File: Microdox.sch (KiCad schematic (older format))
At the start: 47 parts, among them P1 USB, P2 CONN_01X03, SW0:0 SWITCH_DIODE, SW0:1 SWITCH_DIODE, SW0:2 SWITCH_DIODE, SW0:3 SWITCH_DIODE, SW0:4 SWITCH_DIODE, SW0:5 SWITCH_DIODE, SW0:6 SWITCH_DIODE, SW1:0 SWITCH_DIODE, SW1:1 SWITCH_DIODE, SW1:2 SWITCH_DIODE, SW1:3 SWITCH_DIODE, SW1:4 SWITCH_DIODE, SW1:5 SWITCH_DIODE, SW2:0 SWITCH_DIODE, SW2:1 SWITCH_DIODE, SW2:2 SWITCH_DIODE, SW2:3 SWITCH_DIODE, SW2:4 SWITCH_DIODE, SW2:5 SWITCH_DIODE, SW2:6 SWITCH_DIODE, SW3:0 SWITCH_DIODE, SW3:1 SWITCH_DIODE, SW3:2 SWITCH_DIODE, SW3:3 SWITCH_DIODE, SW3:4 SWITCH_DIODE, SW3:5 SWITCH_DIODE, SW3:6 SWITCH_DIODE, SW4:5 SWITCH_DIODE, SW4:6 SWITCH_DIODE

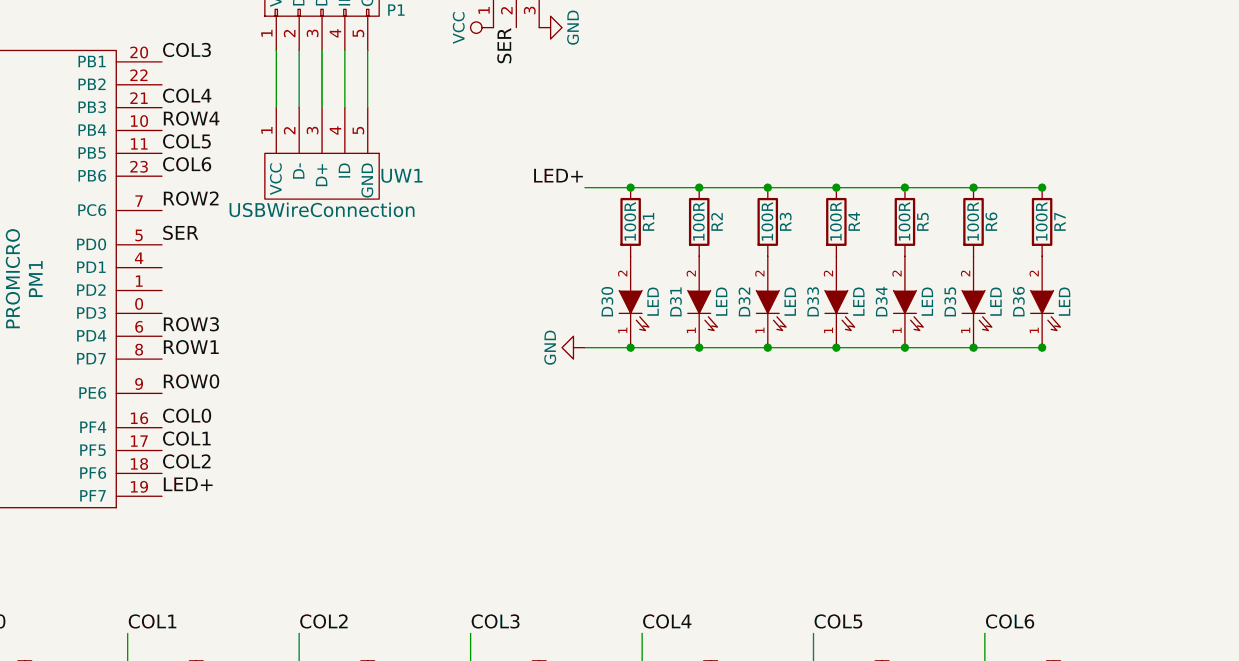
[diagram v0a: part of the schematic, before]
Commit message: Add version without backlighting
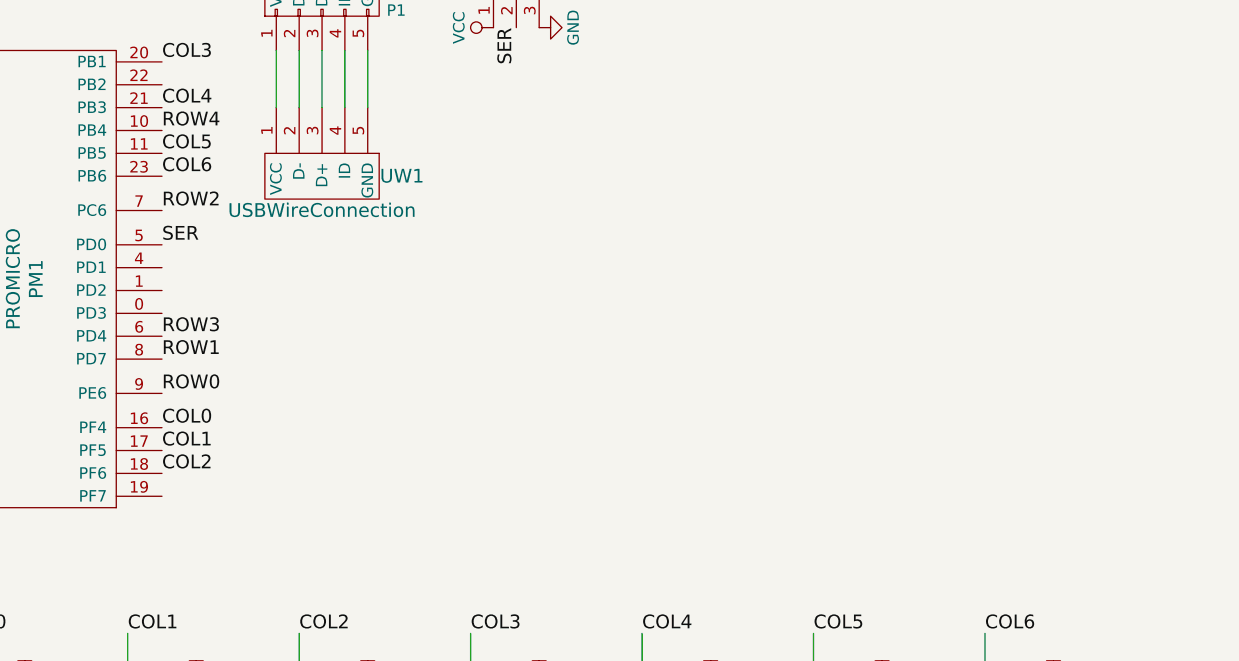
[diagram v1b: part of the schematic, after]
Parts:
- removed D30, D31, D32, D33, D34, D35, D36: LED, LEDs:LED_1206, symbol LED
- removed R1, R2, R3, R4, R5, R6, R7: 100R, Resistors_SMD:R_1206_HandSoldering, symbol R
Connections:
- net LED+: no longer names the net of PM1.19 (PF7)
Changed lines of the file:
@@
 $EndComp
-$Comp
-L LED D30
-U 1 1 56F68FA0
-P 4150 2600
-F 0 "D30" H 4150 2700 50  0000 C CNN
-F 1 "LED" H 4150 2500 50  0000 C CNN
-F 2 "LEDs:LED_1206" H 4150 2600 50  0001 C CNN
-F 3 "" H 4150 2600 50  0000 C CNN
-	1    4150 2600
-	0    -1   -1   0
-$EndComp
-$Comp
-L R R1
-U 1 1 56F6BB88
-P 4150 2250
-F 0 "R1" V 4230 2250 50  0000 C CNN
-F 1 "100R" V 4150 2250 50  0000 C CNN
-F 2 "Resistors_SMD:R_1206_HandSoldering" V 4080 2250 50  0001 C CNN
-F 3 "" H 4150 2250 50  0000 C CNN
-	1    4150 2250
-	1    0    0    -1
-$EndComp
-$Comp
-L LED D31
-U 1 1 56F6D941
-P 4450 2600
-F 0 "D31" H 4450 2700 50  0000 C CNN
-F 1 "LED" H 4450 2500 50  0000 C CNN
-F 2 "LEDs:LED_1206" H 4450 2600 50  0001 C CNN
-F 3 "" H 4450 2600 50  0000 C CNN
-	1    4450 2600
-	0    -1   -1   0
-$EndComp
-$Comp
-L R R2
-U 1 1 56F6D947
-P 4450 2250
-F 0 "R2" V 4530 2250 50  0000 C CNN
-F 1 "100R" V 4450 2250 50  0000 C CNN
-F 2 "Resistors_SMD:R_1206_HandSoldering" V 4380 2250 50  0001 C CNN
-F 3 "" H 4450 2250 50  0000 C CNN
-	1    4450 2250
-	1    0    0    -1
-$EndComp
-$Comp
-L LED D32
-U 1 1 56F6EC9F
-P 4750 2600
-F 0 "D32" H 4750 2700 50  0000 C CNN
-F 1 "LED" H 4750 2500 50  0000 C CNN
-F 2 "LEDs:LED_1206" H 4750 2600 50  0001 C CNN
-F 3 "" H 4750 2600 50  0000 C CNN
-	1    4750 2600
-	0    -1   -1   0
-$EndComp
-$Comp
-L R R3
-U 1 1 56F6ECA5
-P 4750 2250
-F 0 "R3" V 4830 2250 50  0000 C CNN
-F 1 "100R" V 4750 2250 50  0000 C CNN
-F 2 "Resistors_SMD:R_1206_HandSoldering" V 4680 2250 50  0001 C CNN
-F 3 "" H 4750 2250 50  0000 C CNN
-	1    4750 2250
-	1    0    0    -1
-$EndComp
-$Comp
-L LED D33
-U 1 1 56F6ECAD
-P 5050 2600
-F 0 "D33" H 5050 2700 50  0000 C CNN
-F 1 "LED" H 5050 2500 50  0000 C CNN
-F 2 "LEDs:LED_1206" H 5050 2600 50  0001 C CNN
-F 3 "" H 5050 2600 50  0000 C CNN
-	1    5050 2600
-	0    -1   -1   0
-$EndComp
-$Comp
-L R R4
-U 1 1 56F6ECB3
-P 5050 2250
-F 0 "R4" V 5130 2250 50  0000 C CNN
-F 1 "100R" V 5050 2250 50  0000 C CNN
-F 2 "Resistors_SMD:R_1206_HandSoldering" V 4980 2250 50  0001 C CNN
-F 3 "" H 5050 2250 50  0000 C CNN
-	1    5050 2250
-	1    0    0    -1
-$EndComp
-$Comp
-L LED D34
-U 1 1 56F708E7
-P 5350 2600
-F 0 "D34" H 5350 2700 50  0000 C CNN
-F 1 "LED" H 5350 2500 50  0000 C CNN
-F 2 "LEDs:LED_1206" H 5350 2600 50  0001 C CNN
-F 3 "" H 5350 2600 50  0000 C CNN
-	1    5350 2600
-	0    -1   -1   0
-$EndComp
-$Comp
-L R R5
-U 1 1 56F708ED
-P 5350 2250
-F 0 "R5" V 5430 2250 50  0000 C CNN
-F 1 "100R" V 5350 2250 50  0000 C CNN
-F 2 "Resistors_SMD:R_1206_HandSoldering" V 5280 2250 50  0001 C CNN
-F 3 "" H 5350 2250 50  0000 C CNN
-	1    5350 2250
-	1    0    0    -1
-$EndComp
-$Comp
-L LED D35
-U 1 1 56F708F5
-P 5650 2600
-F 0 "D35" H 5650 2700 50  0000 C CNN
-F 1 "LED" H 5650 2500 50  0000 C CNN
-F 2 "LEDs:LED_1206" H 5650 2600 50  0001 C CNN
-F 3 "" H 5650 2600 50  0000 C CNN
-	1    5650 2600
-	0    -1   -1   0
-$EndComp
-$Comp
-L R R6
-U 1 1 56F708FB
-P 5650 2250
-F 0 "R6" V 5730 2250 50  0000 C CNN
-F 1 "100R" V 5650 2250 50  0000 C CNN
-F 2 "Resistors_SMD:R_1206_HandSoldering" V 5580 2250 50  0001 C CNN
-F 3 "" H 5650 2250 50  0000 C CNN
-	1    5650 2250
-	1    0    0    -1
-$EndComp
-$Comp
-L LED D36
-U 1 1 56F70903
-P 5950 2600
-F 0 "D36" H 5950 2700 50  0000 C CNN
-F 1 "LED" H 5950 2500 50  0000 C CNN
-F 2 "LEDs:LED_1206" H 5950 2600 50  0001 C CNN
-F 3 "" H 5950 2600 50  0000 C CNN
-	1    5950 2600
-	0    -1   -1   0
-$EndComp
-$Comp
-L R R7
-U 1 1 56F70909
-P 5950 2250
-F 0 "R7" V 6030 2250 50  0000 C CNN
-F 1 "100R" V 5950 2250 50  0000 C CNN
-F 2 "Resistors_SMD:R_1206_HandSoldering" V 5880 2250 50  0001 C CNN
-F 3 "" H 5950 2250 50  0000 C CNN
-	1    5950 2250
-	1    0    0    -1
-$EndComp
-$Comp
-L GND #PWR07
-U 1 1 56F73DF4
-P 3950 2800
-F 0 "#PWR07" H 3950 2550 50  0001 C CNN
-F 1 "GND" H 3950 2650 50  0000 C CNN
-F 2 "" H 3950 2800 50  0000 C CNN
-F 3 "" H 3950 2800 50  0000 C CNN
-	1    3950 2800
-	0    1    1    0
-$EndComp
-Text Label 3950 2100 2    60   ~ 0
-LED+
-Text Label 2100 3450 0    60   ~ 0
-LED+
 $Comp
 L SWITCH_DIODE SW0:0
@@
 	1    0    0    -1
 $EndComp
-Connection ~ 4150 2800
-Connection ~ 4150 2100
-Connection ~ 4450 2800
-Connection ~ 4450 2100
-Connection ~ 4750 2800
-Connection ~ 4750 2100
-Connection ~ 5050 2800
-Connection ~ 5050 2100
-Connection ~ 5350 2800
-Connection ~ 5350 2100
-Connection ~ 5650 2800
-Connection ~ 5650 2100
-Connection ~ 5950 2800
-Connection ~ 5950 2100
 Wire Wire Line
 	1800 4300 1800 4250
@@
 Text Label 6600 7100 0    60   ~ 0
 ROW4
-Wire Wire Line
-	3950 2100 5950 2100
-Wire Wire Line
-	3950 2800 5950 2800
 $Comp
 L USB_OTG P1

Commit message: Add more vias
Fix non-connectivity island
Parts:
- added SWR1: SW_PUSH, Buttons_Switches_ThroughHole:SW_Tactile_SPST_Angled, symbol SW_PUSH
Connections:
- new net Earth: SWR1.2
- new net RST: SWR1.1
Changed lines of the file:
@@
 $EndComp
 $Comp
-L GND #PWR08
+L GND #PWR07
 U 1 1 56F1AFF1
 P 3200 1100
-F 0 "#PWR08" H 3200 850 50  0001 C CNN
+F 0 "#PWR07" H 3200 850 50  0001 C CNN
 F 1 "GND" H 3200 950 50  0000 C CNN
 F 2 "" H 3200 1100 50  0000 C CNN
@@
 	1    0    0    -1
 $EndComp
+$Comp
+L SW_PUSH SWR1
+U 1 1 572E2571
+P 4550 2500
+F 0 "SWR1" H 4700 2610 50  0000 C CNN
+F 1 "SW_PUSH" H 4550 2420 50  0000 C CNN
+F 2 "Buttons_Switches_ThroughHole:SW_Tactile_SPST_Angled" H 4550 2500 50  0001 C CNN
+F 3 "" H 4550 2500 50  0000 C CNN
+	1    4550 2500
+	1    0    0    -1
+$EndComp
+$Comp
+L Earth #PWR08
+U 1 1 572E3FEC
+P 4850 2500
+F 0 "#PWR08" H 4850 2250 50  0001 C CNN
+F 1 "Earth" H 4850 2350 50  0001 C CNN
+F 2 "" H 4850 2500 50  0000 C CNN
+F 3 "" H 4850 2500 50  0000 C CNN
+	1    4850 2500
+	0    -1   -1   0
+$EndComp
+Text Label 4000 2500 0    60   ~ 0
+RST
+Wire Wire Line
+	4000 2500 4250 2500
 $EndSCHEMATC

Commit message: Add proper 3.5mm jack pins
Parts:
- P2: footprint Pin_Headers:Pin_Header_Angled_1x03 -> Keyboards:3mmJack
- SWR1: footprint Buttons_Switches_ThroughHole:SW_Tactile_SPST_Angled -> Buttons_Switches_ThroughHole:SW_TH_Tactile_Omron_B3F-10xx
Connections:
- net Earth is gone; now on net GND: SWR1.2
- net ROW1: now also SW2:6.4 (K)
- net ROW2: no longer SW2:6.4 (K)
- net RST: now also PM1.14 (RST)
- no-connect marks 1 -> 0
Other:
- moved on the sheet: SW2:6
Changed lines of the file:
@@
 	0    1    1    0
 $EndComp
-NoConn ~ 900  1550
 $Comp
 L GND #PWR05
@@
 F 0 "P2" H 3650 1400 50  0000 C CNN
 F 1 "CONN_01X03" V 3750 1200 50  0000 C CNN
-F 2 "Pin_Headers:Pin_Header_Angled_1x03" H 3650 1200 50  0001 C CNN
+F 2 "Keyboards:3mmJack" H 3650 1200 50  0001 C CNN
 F 3 "" H 3650 1200 50  0000 C CNN
 	1    3650 1200
@@
 L SWITCH_DIODE SW2:6
 U 1 1 56ED6EBF
-P 6000 5450
-F 0 "SW2:6" H 6000 5250 60  0000 C CNN
-F 1 "SWITCH_DIODE" H 6000 5350 39  0000 C CNN
-F 2 "Keyboards:MX_FLIP_DIODE" H 6000 5450 60  0001 C CNN
-F 3 "" H 6000 5450 60  0000 C CNN
-	1    6000 5450
+P 6000 4850
+F 0 "SW2:6" H 6000 4650 60  0000 C CNN
+F 1 "SWITCH_DIODE" H 6000 4750 39  0000 C CNN
+F 2 "Keyboards:MX_FLIP_DIODE" H 6000 4850 60  0001 C CNN
+F 3 "" H 6000 4850 60  0000 C CNN
+	1    6000 4850
 	1    0    0    -1
 $EndComp
@@
 Wire Wire Line
 	1800 5900 6600 5900
-Wire Wire Line
-	6300 5500 6300 5450
-Connection ~ 5700 5450
-Connection ~ 6300 5900
 $Comp
 L SWITCH_DIODE SW3:0
@@
 F 0 "SWR1" H 4700 2610 50  0000 C CNN
 F 1 "SW_PUSH" H 4550 2420 50  0000 C CNN
-F 2 "Buttons_Switches_ThroughHole:SW_Tactile_SPST_Angled" H 4550 2500 50  0001 C CNN
+F 2 "Buttons_Switches_ThroughHole:SW_TH_Tactile_Omron_B3F-10xx" H 4550 2500 50  0001 C CNN
 F 3 "" H 4550 2500 50  0000 C CNN
 	1    4550 2500
 	1    0    0    -1
 $EndComp
-$Comp
-L Earth #PWR08
-U 1 1 572E3FEC
+Text Label 4000 2500 0    60   ~ 0
+RST
+Wire Wire Line
+	4000 2500 4250 2500
+Wire Wire Line
+	6300 4850 6300 4900
+Connection ~ 6300 5300
+Connection ~ 5700 4850
+$Comp
+L GND #PWR08
+U 1 1 5778D2D1
 P 4850 2500
 F 0 "#PWR08" H 4850 2250 50  0001 C CNN
-F 1 "Earth" H 4850 2350 50  0001 C CNN
+F 1 "GND" H 4850 2350 50  0000 C CNN
 F 2 "" H 4850 2500 50  0000 C CNN
 F 3 "" H 4850 2500 50  0000 C CNN
@@
 	0    -1   -1   0
 $EndComp
-Text Label 4000 2500 0    60   ~ 0
+Text Label 900  1550 2    60   ~ 0
 RST
-Wire Wire Line
-	4000 2500 4250 2500
 $EndSCHEMATC
